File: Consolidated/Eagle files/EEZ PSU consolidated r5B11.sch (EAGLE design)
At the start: 545 parts, among them IC1 LTC3864EMSE#PBF, IC10 REF5025AIDG4, IC11 DAC8552IDGKTG4, IC12 ADG465SOT-23, IC13 TS5A9411DCKT, IC14 ADS1120IPWR, IC15 LP339D, IC16 LM25575MH/NOPB, IC17 TPD4E002DRLR, IC18 TPD2E001DZDR, IC19 ADUM3160BRWZ, IC2 MC79L05, IC20 TLC5925IDBQR, IC21 Si8641EC-B-IS1, IC22 SI8651EC-B-IS1, IC23 SI8651EC-B-IS1, IC24 LD1117ADT33TR, IC25 Si8641EC-B-IS1, IC26 PCA21125T/Q900/1,1, IC27 AT25256B-SSHL-B, IC28 W5500, IC29 BC857BS, IC3 MC78L05, IC30 TLC555, IC31 SN74LVC08APWR, IC32 TPS3705-33D, IC33 SN74LV1T34DBVR, IC34 SN74LVC2G02DCTR, IC4 LM5574MTX/NOPB, IC5 LP2951SO8, IC6 TL072D, IC7 TL072D, IC8 OP27GSZ, IC9 MCP23S08-E/SO, J1 BS-244DSM-R, J2 BS-244DSM-G, J3 BS-244DSM-B, J4 BS-244DSM-R, J5 BS-244DSM-B, J6 1-726388-2, Q1 IRFR5305, Q10 MMBT5401, Q11 MMBT5401, Q12 MMBT5551, Q13 MMBT5551, Q14 BSS84P, Q15 2N7002, Q16 MMBT5551, Q17 MMBT5401, Q18 MMBT5551, Q19 MMBT5551, Q2 MMBT5401, Q20 BTA26-600, Q21 BTA26-600, Q22 IRLL014N, Q23 IRLML2246TRPBF, Q24 IRLML2246TRPBF, Q25 IRLML2246TRPBF, Q26 IRLML2246TRPBF, Q27 2N7002, Q28 IRLML2246TRPBF, Q29 2N7002, Q3 2N7002, Q30 2N7002, Q4 IRFP250N, Q5 BC857C, Q7 BCP56-16.115, Q8 IRFR5305, Q9 BCP56-16.115, SW1 A101SYCQ04, SW2 1301.9316, X1 39303035, X10 826629-5, X11 2411-01, X12 MC000006, X13 TSW-113-07-F-D, X14 MC000005, X15 TSW-113-07-F-D, X16 09185067324, X17 22-23-2021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

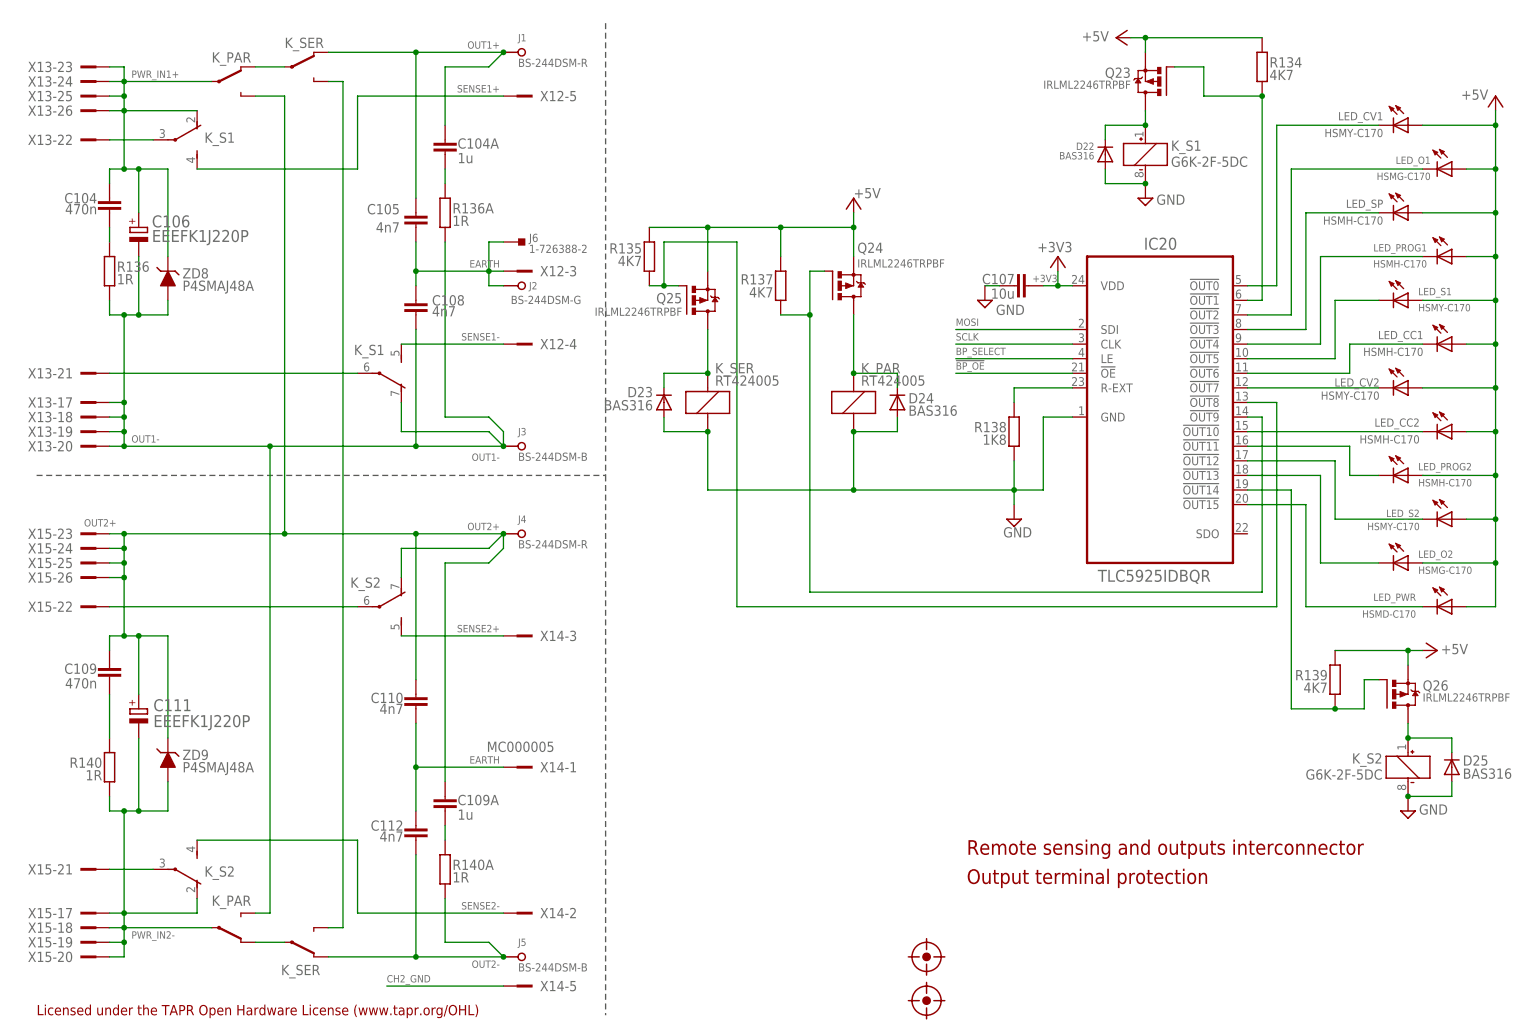
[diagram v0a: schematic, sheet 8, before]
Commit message: optimized values for CC resistors
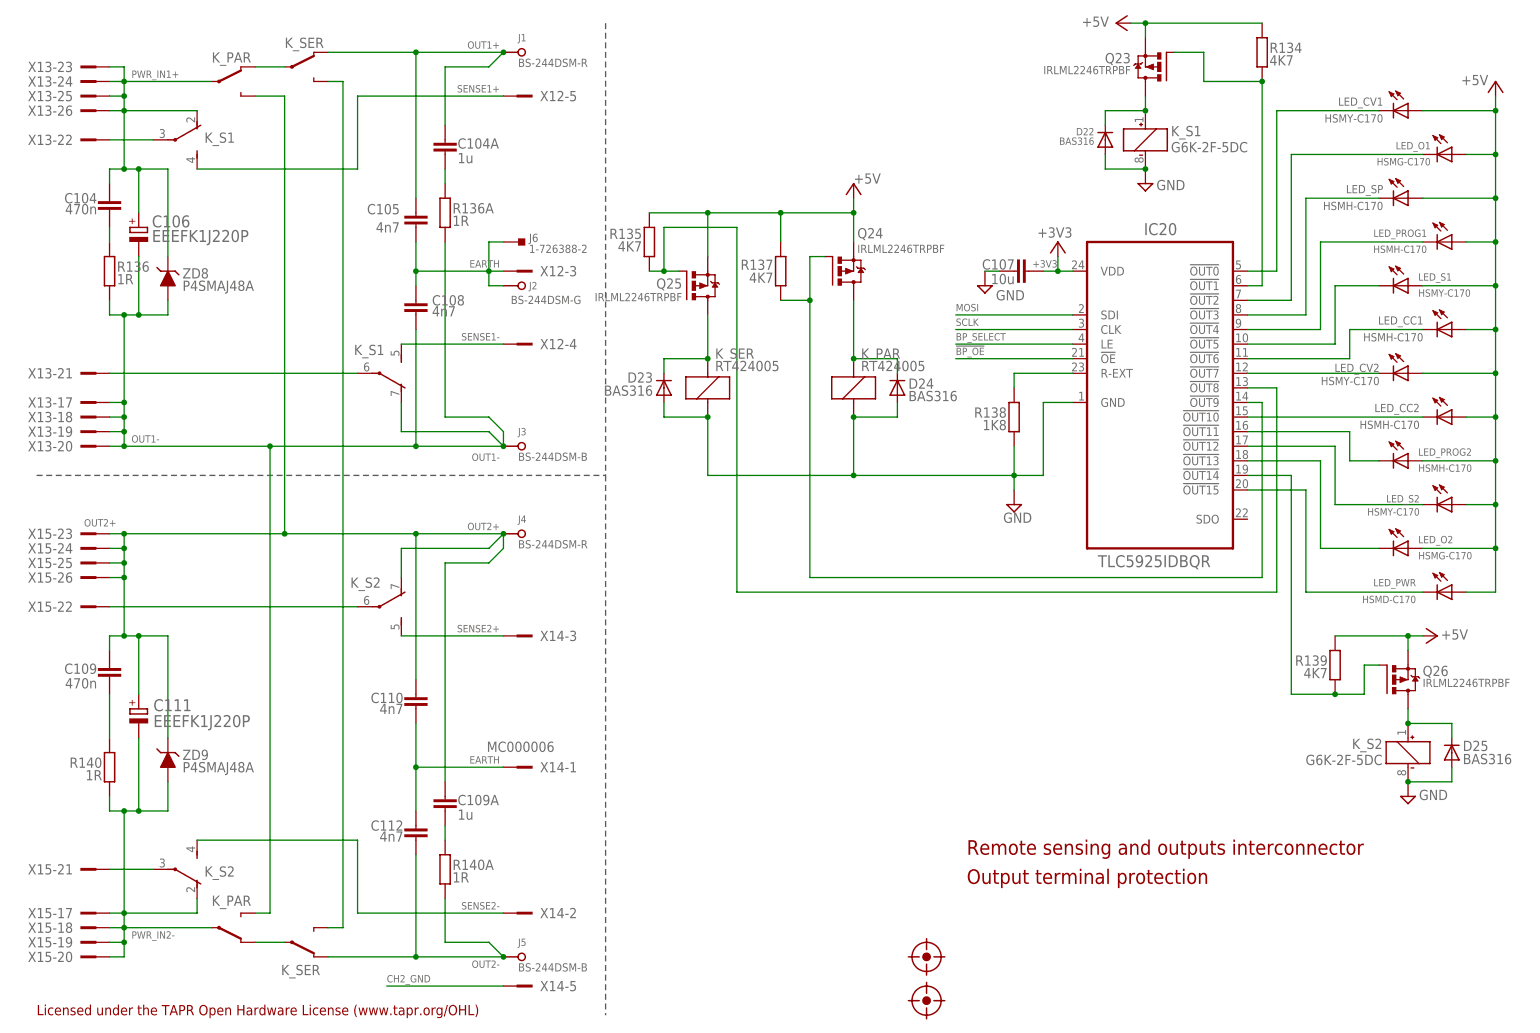
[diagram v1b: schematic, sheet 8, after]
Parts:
- C95: value 3n9 -> 3n3
- R32: value 2K2 -> 1K
- R64, R72: value 2K55 0.1% -> 2K 0.1%
- R67, R71: value 102R 0.1% -> 82R 0.1%
- R70: value 5K1 -> 10K
- X14: value MC000005 -> MC000006
- Y1: value 32,768kHz -> 32.768kHz
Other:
- note added: "+50 mV"
- note added: "16K"
- note added: "22K"
- note added: "2K"
- note added: "2K74"
- note added: "3K24"
- note added: "Note 10.1: Solder LCD1 socket on the PCB's opposite side"
- note added: "Note 11.1: Solder SW2 on the PCB's opposite side"
- note added: "Note 8.1: Solder (or insert into socket!) X12 and X14 on the PCB's opposite side"
- note added: "Note 8.2: Solder all LEDs on the PCB's opposite side"
- note added: "Note 9.1: Solder SW1 on the PCB's opposite side"
- note added: "R47, R57"
- note removed: "+100mV"
- note removed: "15K / 16K"
- note removed: "20K / 22K"
- note removed: "2K55"
- note removed: "3K42"
- note removed: "4K08"
- note removed: "Note 8.1: Solder X1 and X3 on the PCB's opposite side"
- note removed: "R47, R57 / ext.range"
- note removed: "Solder LCD1 socket on the PCB's opposite side"
- moved on the sheet: C107, D22, D23, D24, D25, IC20, K_PAR, K_S1, K_S2, K_SER, LED_CC1, LED_CC2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

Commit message: #16, #17, #18
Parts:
- added C153, C157: 50SVPF18M, Panasonic-EEEFK_EEEFP:EEE-FK1J220P-CASE-E
- added C161: 4n7, rcl:C-EUC1210
- C106, C111: value EEEFK1J220P -> EEEFK1H470P
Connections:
- net N$68 renamed AUX_SYNC
- net +3V3: now also C125.2, SP1.+
- net +5V: no longer C125.2, SP1.+
- net AC_EARTH: now also C161.1
- net AUX2_USET_IN: now also X14-8.1; no longer X14-6.1
- net CH2_GND: now also X14-7.1; no longer X14-5.1
- net EARTH: now also X14-3.1; no longer X14-1.1
- net GND: now also C161.2
- net N$188: now also X14-2.1; no longer X14-8.1
- net N$189: now also X14-1.1; no longer X14-7.1
- net OUT1+: now also C153.1; no longer C105.1
- net OUT1-: now also C153.2
- net OUT2+: now also C157.1
- net OUT2-: now also C157.2; no longer C112.2
- net PWR_IN1+: now also C105.1
- net PWR_IN2-: now also C112.2
- net SENSE2+: now also X14-5.1; no longer X14-3.1
- net SENSE2-: now also X14-4.1; no longer X14-2.1
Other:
- moved on the sheet: C104, C105, C106, C108, C109, C110, C111, C112, R136, R136A, R140, X12-8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
